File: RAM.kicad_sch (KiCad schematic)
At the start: 286 parts, among them J1 Conn_01x50, J2 JTAG_01x06, J3 Conn_01x03_Male, U10 W25Q128JVS, U11 TPS62823DLC, U12 TPS62823DLC, U13 TPS62823DLC, U14 TPS62823DLC, U16 TPS62823DLC, U17 Si52112-B5-GM2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

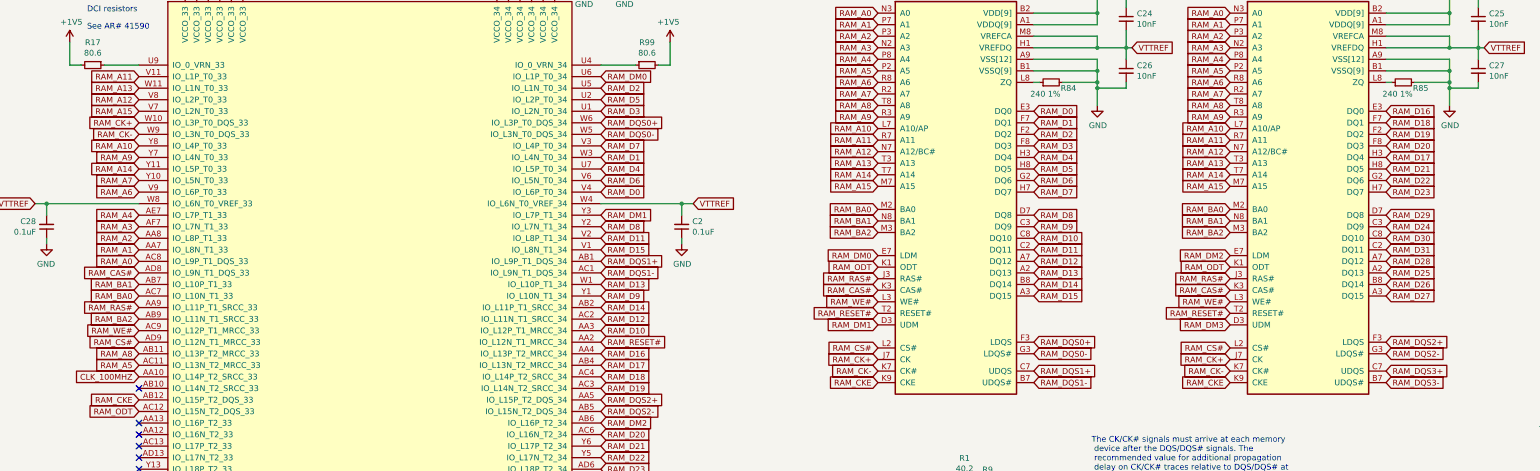
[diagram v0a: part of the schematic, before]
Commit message: ddr new routing snapshot before length matching
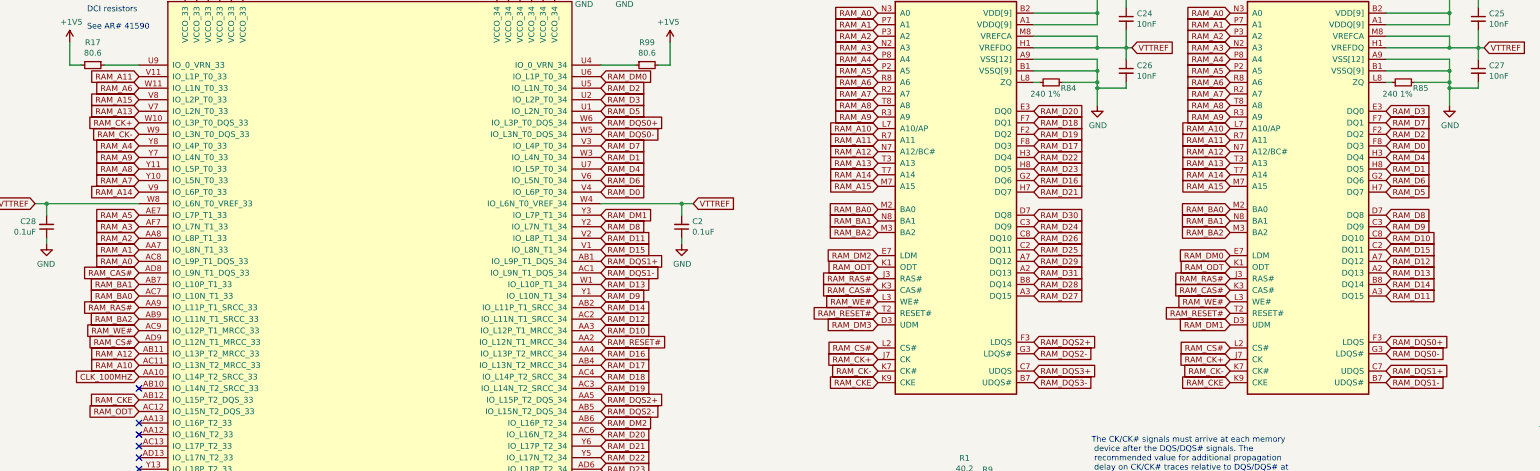
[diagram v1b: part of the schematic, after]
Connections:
- net RAM_A10: now also U2.AC11 (IO_L13N_T2_MRCC_33); no longer U2.Y8 (IO_L4P_T0_33)
- net RAM_A12: now also U2.AB11 (IO_L13P_T2_MRCC_33); no longer U2.V8 (IO_L2P_T0_33)
- net RAM_A13: now also U2.V7 (IO_L2N_T0_33); no longer U2.W11 (IO_L1N_T0_33)
- net RAM_A14: now also U2.V9 (IO_L6P_T0_33); no longer U2.Y11 (IO_L5P_T0_33)
- net RAM_A15: now also U2.V8 (IO_L2P_T0_33); no longer U2.V7 (IO_L2N_T0_33)
- net RAM_A4: now also U2.Y8 (IO_L4P_T0_33); no longer U2.AE7 (IO_L7P_T1_33)
- net RAM_A5: now also U2.AE7 (IO_L7P_T1_33); no longer U2.AC11 (IO_L13N_T2_MRCC_33)
- net RAM_A6: now also U2.W11 (IO_L1N_T0_33); no longer U2.V9 (IO_L6P_T0_33)
- net RAM_A8: now also U2.Y11 (IO_L5P_T0_33); no longer U2.AB11 (IO_L13P_T2_MRCC_33)
- net RAM_D0: now also U4.F8 (DQ3); no longer U3.E3 (DQ0)
- net RAM_D1: now also U4.H8 (DQ5); no longer U3.F7 (DQ1)
- net RAM_D10: now also U4.C8 (DQ10); no longer U3.C8 (DQ10)
- net RAM_D11: now also U4.A3 (DQ15); no longer U3.C2 (DQ11)
- net RAM_D12: now also U4.A7 (DQ12); no longer U3.A7 (DQ12)
- net RAM_D13: now also U4.A2 (DQ13); no longer U3.A2 (DQ13)
- net RAM_D14: now also U4.B8 (DQ14); no longer U3.B8 (DQ14)
- net RAM_D15: now also U4.C2 (DQ11); no longer U3.A3 (DQ15)
- net RAM_D16: now also U3.G2 (DQ6); no longer U4.E3 (DQ0)
- net RAM_D17: now also U3.F8 (DQ3); no longer U4.H3 (DQ4)
- net RAM_D18: now also U3.F7 (DQ1); no longer U4.F7 (DQ1)
- net RAM_D19: now also U3.F2 (DQ2); no longer U4.F2 (DQ2)
- net RAM_D2: now also U4.F2 (DQ2); no longer U3.F2 (DQ2)
- net RAM_D20: now also U3.E3 (DQ0); no longer U4.F8 (DQ3)
- net RAM_D21: now also U3.H7 (DQ7); no longer U4.H8 (DQ5)
- net RAM_D22: now also U3.H3 (DQ4); no longer U4.G2 (DQ6)
- net RAM_D23: now also U3.H8 (DQ5); no longer U4.H7 (DQ7)
- net RAM_D24: now also U3.C3 (DQ9); no longer U4.C3 (DQ9)
- net RAM_D25: now also U3.C2 (DQ11); no longer U4.A2 (DQ13)
- net RAM_D26: now also U3.C8 (DQ10); no longer U4.B8 (DQ14)
- net RAM_D27: now also U3.A3 (DQ15); no longer U4.A3 (DQ15)
- net RAM_D28: now also U3.B8 (DQ14); no longer U4.A7 (DQ12)
- net RAM_D29: now also U3.A7 (DQ12); no longer U4.D7 (DQ8)
- net RAM_D3: now also U2.U2 (IO_L2P_T0_34), U4.E3 (DQ0); no longer U2.U1 (IO_L2N_T0_34), U3.F8 (DQ3)
- net RAM_D30: now also U3.D7 (DQ8); no longer U4.C8 (DQ10)
- net RAM_D31: now also U3.A2 (DQ13); no longer U4.C2 (DQ11)
- net RAM_D4: now also U4.H3 (DQ4); no longer U3.H3 (DQ4)
- net RAM_D5: now also U2.U1 (IO_L2N_T0_34), U4.H7 (DQ7); no longer U2.U2 (IO_L2P_T0_34), U3.H8 (DQ5)
- net RAM_D6: now also U4.G2 (DQ6); no longer U3.G2 (DQ6)
- net RAM_D7: now also U4.F7 (DQ1); no longer U3.H7 (DQ7)
- net RAM_D8: now also U4.D7 (DQ8); no longer U3.D7 (DQ8)
- net RAM_D9: now also U4.C3 (DQ9); no longer U3.C3 (DQ9)
- net RAM_DM0: now also U4.E7 (LDM); no longer U3.E7 (LDM)
- net RAM_DM1: now also U4.D3 (UDM); no longer U3.D3 (UDM)
- net RAM_DM2: now also U3.E7 (LDM); no longer U4.E7 (LDM)
- net RAM_DM3: now also U3.D3 (UDM); no longer U4.D3 (UDM)
- net RAM_DQS0+: now also U4.F3 (LDQS); no longer U3.F3 (LDQS)
- net RAM_DQS0-: now also U4.G3 (LDQS#); no longer U3.G3 (LDQS#)
- net RAM_DQS1+: now also U4.C7 (UDQS); no longer U3.C7 (UDQS)
- net RAM_DQS1-: now also U4.B7 (UDQS#); no longer U3.B7 (UDQS#)
- net RAM_DQS2+: now also U3.F3 (LDQS); no longer U4.F3 (LDQS)
- net RAM_DQS2-: now also U3.G3 (LDQS#); no longer U4.G3 (LDQS#)
- net RAM_DQS3+: now also U3.C7 (UDQS); no longer U4.C7 (UDQS)
- net RAM_DQS3-: now also U3.B7 (UDQS#); no longer U4.B7 (UDQS#)

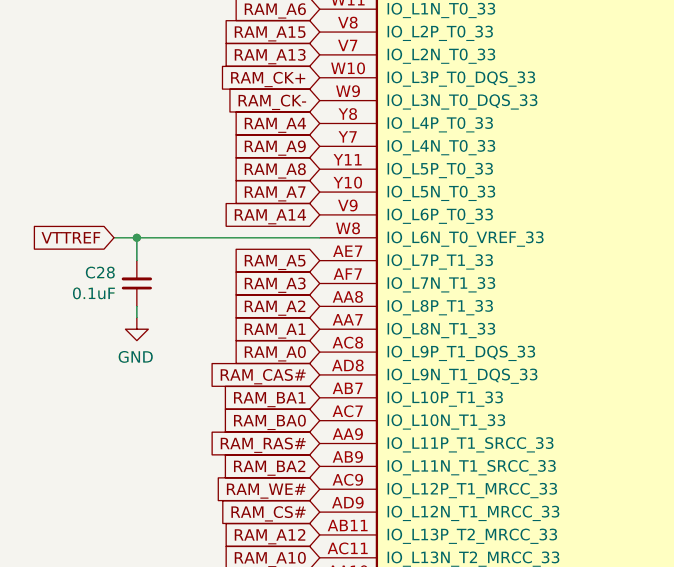
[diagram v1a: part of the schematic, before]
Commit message: ddr new routing snapshot after length matching
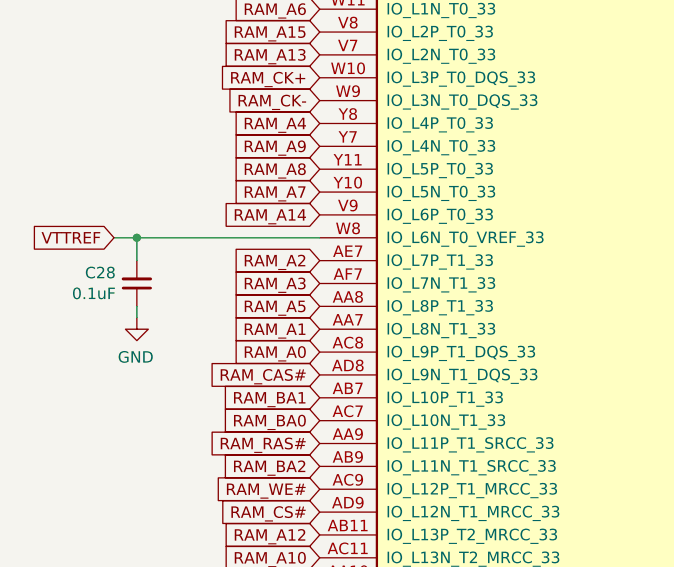
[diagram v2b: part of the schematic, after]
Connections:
- net RAM_A2: now also U2.AE7 (IO_L7P_T1_33); no longer U2.AA8 (IO_L8P_T1_33)
- net RAM_A5: now also U2.AA8 (IO_L8P_T1_33); no longer U2.AE7 (IO_L7P_T1_33)
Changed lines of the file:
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@@
     )
   )
-  (global_label "RAM_A5" (shape input) (at 76.2 312.42 180) (fields_autoplaced)
-    (effects (font (size 1.27 1.27)) (justify right))
-    (property "Intersheet References" "${INTERSHEET_REFS}" (id 0) (at 0 -33.02 0)
+  (global_label "RAM_A5" (shape input) (at 76.2 317.5 180) (fields_autoplaced)
+    (effects (font (size 1.27 1.27)) (justify right))
+    (property "Intersheet References" "${INTERSHEET_REFS}" (id 0) (at 0 -27.94 0)
       (effects (font (size 1.27 1.27)) hide)
     )
@@
     )
   )
-  (global_label "RAM_A2" (shape input) (at 76.2 317.5 180) (fields_autoplaced)
-    (effects (font (size 1.27 1.27)) (justify right))
-    (property "Intersheet References" "${INTERSHEET_REFS}" (id 0) (at 0 0 0)
-      (effects (font (size 1.27 1.27)) hide)
-    )
+  (global_label "RAM_A2" (shape input) (at 76.2 312.42 180) (fields_autoplaced)
+    (effects (font (size 1.27 1.27)) (justify right))
+    (property "Intersheet References" "${INTERSHEET_REFS}" (id 0) (at 0 -5.08 0)
+      (effects (font (size 1.27 1.27)) hide)
+    )

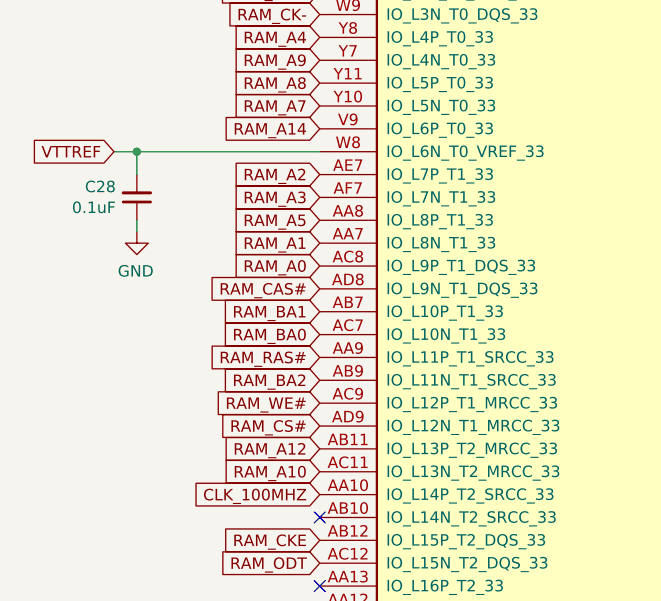
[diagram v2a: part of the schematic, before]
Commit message: snapshot with tuned ddr address/command group
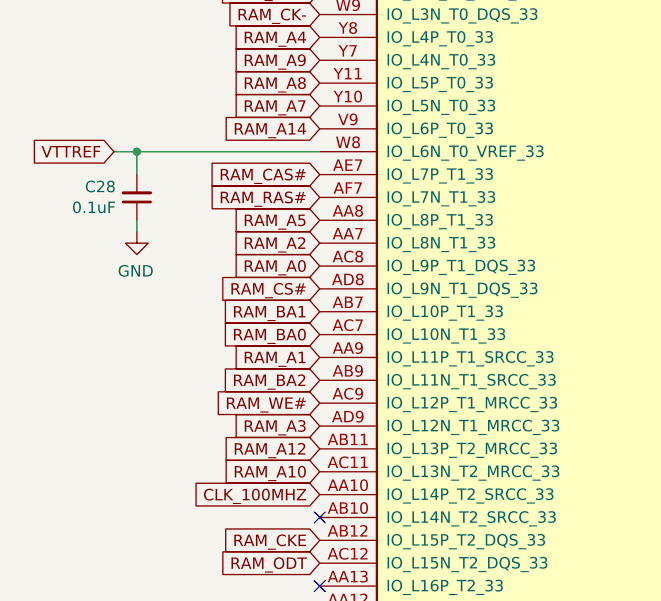
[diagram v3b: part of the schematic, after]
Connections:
- net RAM_A1: now also U2.AA9 (IO_L11P_T1_SRCC_33); no longer U2.AA7 (IO_L8N_T1_33)
- net RAM_A2: now also U2.AA7 (IO_L8N_T1_33); no longer U2.AE7 (IO_L7P_T1_33)
- net RAM_A3: now also U2.AD9 (IO_L12N_T1_MRCC_33); no longer U2.AF7 (IO_L7N_T1_33)
- net RAM_CAS#: now also U2.AE7 (IO_L7P_T1_33); no longer U2.AD8 (IO_L9N_T1_DQS_33)
- net RAM_CS#: now also U2.AD8 (IO_L9N_T1_DQS_33); no longer U2.AD9 (IO_L12N_T1_MRCC_33)
- net RAM_RAS#: now also U2.AF7 (IO_L7N_T1_33); no longer U2.AA9 (IO_L11P_T1_SRCC_33)
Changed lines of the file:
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@@
     )
   )
-  (global_label "RAM_CS#" (shape input) (at 76.2 340.36 180) (fields_autoplaced)
-    (effects (font (size 1.27 1.27)) (justify right))
-    (property "Intersheet References" "${INTERSHEET_REFS}" (id 0) (at 0 0 0)
+  (global_label "RAM_CS#" (shape input) (at 76.2 325.12 180) (fields_autoplaced)
+    (effects (font (size 1.27 1.27)) (justify right))
+    (property "Intersheet References" "${INTERSHEET_REFS}" (id 0) (at 0 -15.24 0)
       (effects (font (size 1.27 1.27)) hide)
     )
@@
     )
   )
-  (global_label "RAM_RAS#" (shape input) (at 76.2 332.74 180) (fields_autoplaced)
-    (effects (font (size 1.27 1.27)) (justify right))
-    (property "Intersheet References" "${INTERSHEET_REFS}" (id 0) (at 0 0 0)
+  (global_label "RAM_RAS#" (shape input) (at 76.2 314.96 180) (fields_autoplaced)
+    (effects (font (size 1.27 1.27)) (justify right))
+    (property "Intersheet References" "${INTERSHEET_REFS}" (id 0) (at 0 -17.78 0)
       (effects (font (size 1.27 1.27)) hide)
     )
@@
     )
   )
-  (global_label "RAM_A1" (shape input) (at 76.2 320.04 180) (fields_autoplaced)
-    (effects (font (size 1.27 1.27)) (justify right))
-    (property "Intersheet References" "${INTERSHEET_REFS}" (id 0) (at 0 0 0)
-      (effects (font (size 1.27 1.27)) hide)
-    )
-  )
-  (global_label "RAM_CAS#" (shape input) (at 76.2 325.12 180) (fields_autoplaced)
-    (effects (font (size 1.27 1.27)) (justify right))
-    (property "Intersheet References" "${INTERSHEET_REFS}" (id 0) (at 0 0 0)
+  (global_label "RAM_A1" (shape input) (at 76.2 332.74 180) (fields_autoplaced)
+    (effects (font (size 1.27 1.27)) (justify right))
+    (property "Intersheet References" "${INTERSHEET_REFS}" (id 0) (at 0 12.7 0)
+      (effects (font (size 1.27 1.27)) hide)
+    )
+  )
+  (global_label "RAM_CAS#" (shape input) (at 76.2 312.42 180) (fields_autoplaced)
+    (effects (font (size 1.27 1.27)) (justify right))
+    (property "Intersheet References" "${INTERSHEET_REFS}" (id 0) (at 0 -12.7 0)
       (effects (font (size 1.27 1.27)) hide)
     )
@@
     )
   )
-  (global_label "RAM_A2" (shape input) (at 76.2 312.42 180) (fields_autoplaced)
-    (effects (font (size 1.27 1.27)) (justify right))
-    (property "Intersheet References" "${INTERSHEET_REFS}" (id 0) (at 0 -5.08 0)
+  (global_label "RAM_A2" (shape input) (at 76.2 320.04 180) (fields_autoplaced)
+    (effects (font (size 1.27 1.27)) (justify right))
+    (property "Intersheet References" "${INTERSHEET_REFS}" (id 0) (at 0 2.54 0)
       (effects (font (size 1.27 1.27)) hide)
     )
@@
     )
   )
-  (global_label "RAM_A3" (shape input) (at 76.2 314.96 180) (fields_autoplaced)
-    (effects (font (size 1.27 1.27)) (justify right))
-    (property "Intersheet References" "${INTERSHEET_REFS}" (id 0) (at 0 0 0)
-      (effects (font (size 1.27 1.27)) hide)
-    )
+  (global_label "RAM_A3" (shape input) (at 76.2 340.36 180) (fields_autoplaced)
+    (effects (font (size 1.27 1.27)) (justify right))
+    (property "Intersheet References" "${INTERSHEET_REFS}" (id 0) (at 0 25.4 0)
+      (effects (font (size 1.27 1.27)) hide)
+    )

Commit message: snapshot after cleanup
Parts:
- removed C31, C34: 10uF, symbol Device:C_Small
- removed C32: 0.1uF, Capacitor_SMD:C_0402_1005Metric, symbol Device:C_Small
- removed C33: 3.3nF, Capacitor_SMD:C_0402_1005Metric, symbol Device:C_Small
- removed L7: IHLP1212AEERR47M11, Inductor_SMD:L_Vishay_IHLP-1212, symbol Device:L_Small
- removed R52, R56: 100k 1%, Resistor_SMD:R_0402_1005Metric, symbol Device:R_Small
- removed R53: 32k 1%, Resistor_SMD:R_0402_1005Metric, symbol Device:R_Small
- removed U7: TPS62131, Package_DFN_QFN:VQFN-16-1EP_3x3mm_P0.5mm_EP1.68x1.68mm_ThermalVias, symbol Regulator_Switching:TPS62131
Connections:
- net +1V2: no longer J1.35 (Pin_35), J1.36 (Pin_36)
- net +1V8: now also J1.35 (Pin_35), J1.36 (Pin_36)
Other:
- note removed: "2.2uH?"
- note removed: "22uF?"
- note removed: "Formula: R1 = R2 x (Vout/0.8 - 1) R2 should not exceed 400 kΩ"

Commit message: first finished layout of rev 2
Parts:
- added C15, C31, C32: 0.1uF, Capacitor_SMD:C_0402_1005Metric, symbol Device:C_Small
- added R44, R45: 0, Resistor_SMD:R_0402_1005Metric, symbol Device:R_Small
- added R52, R53: 100k 1%, Resistor_SMD:R_0402_1005Metric, symbol Device:R_Small
- added TP10, TP11, TP12, TP14, TP15, TP16, TP2, TP8, TP9: TestPoint, TestPoint:TestPoint_Pad_1.0x1.0mm, symbol Connector:TestPoint
- J2: footprint Connector_PinHeader_2.00mm:PinHeader_1x06_P2.00mm_Horizontal -> Connector_PinHeader_2.00mm:PinHeader_1x06_P2.00mm_Vertical
- J3: footprint Connector_PinHeader_2.00mm:PinHeader_1x03_P2.00mm_Horizontal -> Connector_PinHeader_2.00mm:PinHeader_1x03_P2.00mm_Vertical
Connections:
- net +5V: now also R52.1, R53.1
- net DISP2_GPIO0: now also U2.N21 (IO_L12P_T1_MRCC_13)
- net DISP2_GPIO1: now also U2.N19 (IO_L7P_T1_13)
- net DISP2_GPIO2: now also U2.M19 (IO_L22N_T3_13)
- net DISP2_GPIO3: now also U2.M20 (IO_L7N_T1_13)
- net DISP2_GPIO4: now also U2.M21 (IO_L10P_T1_13)
- net DISP2_GPIO5: now also U2.M22 (IO_L10N_T1_13)
- net EN_VDDR: now also R52.2
- net EN_VIO: now also R53.2
- net GND: now also C32.2, TP16.1
- net USB1_RX_P: now reaches U2.K25 (IO_L1P_T0_13)
- net USB1_RX_N: now reaches U2.K26 (IO_L1N_T0_13)
- net USB1_C_DN: now reaches U2.L24 (IO_L8N_T1_13)
- net USB1_C_DN: now also R45.2
- net USB1_C_DP: now reaches U2.M24 (IO_L8P_T1_13)
- net USB1_C_DP: now also R44.1
- net USB1_TX_CN: now reaches U2.M26 (IO_L5N_T0_13)
- net USB1_TX_CN: now also C15.2
- net USB1_TX_CP: now reaches U2.N26 (IO_L5P_T0_13)
- net USB1_TX_CP: now also C31.2
- net TP_P21: now reaches U2.P21 (IO_L13N_T2_MRCC_13)
- net TP_P21: now also TP15.1
- net TP_P26: now reaches U2.P26 (IO_L2N_T0_13)
- net TP_P26: now also TP10.1
- net TP_R21: now reaches U2.R21 (IO_L13P_T2_MRCC_13)
- net TP_R21: now also TP14.1
- net TP_R23: now reaches U2.R23 (IO_L14N_T2_SRCC_13)
- net TP_R23: now also TP12.1
- net TP_R26: now reaches U2.R26 (IO_L2P_T0_13)
- net TP_R26: now also TP11.1
- net TP_U26: now reaches U2.U26 (IO_L4P_T0_12)
- net TP_U26: now also TP9.1
- net TP_V26: now reaches U2.V26 (IO_L4N_T0_12)
- net TP_V26: now also TP8.1
- net TP_W25: now reaches U2.W25 (IO_L5P_T0_12)
- net TP_W25: now also TP2.1
- net at R101.2, U18.3 (EN): now also C32.1
- net EN_VAUX: no longer names the net of U18.6 (FLAG1)
- new net USB1_DN: R45.1
- new net USB1_DP: R44.2
- new net USB1_TX_N: C15.1
- new net USB1_TX_P: C31.1
- no-connect marks 183 -> 180
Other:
- note added: "POWERUP SEQUENCER"
- note added: "TODO: might need to SWAP a SATA pair!?!"
- note removed: "TODO: resolve bodges"
- note removed: "ball assignments checked, except power"
- moved on the sheet: R101, U18

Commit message: pcb: clean up D-2 BOM
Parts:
- added R46: 1.5k, Resistor_SMD:R_0402_1005Metric, symbol Device:R_Small
- C82, C89, C93, C94, C97, C98: Manufacturer (none) -> Generic; Manufacturer_No (none) -> 0603 10V+
- D1, D2: Manufacturer (none) -> Generic; Manufacturer_No (none) -> WLED 0603
- FB1, FB2, FB3: Manufacturer (none) -> Murata; Manufacturer_No (none) -> 100ohms @ 100MHz 0603
- GFX2: footprint footprints:mnt-rkx7-badge-d01 -> footprints:mnt-rkx7-badge-d02
- J1: Manufacturer (none) -> Hirose; Manufacturer_No (none) -> FH12-50S-0.5SH
- R101, R32, R35, R38, R41, R47: Manufacturer (none) -> Yageo; Manufacturer_No (none) -> AC0402FR-070RL
- R36: Manufacturer (none) -> Vishay Dale; Manufacturer_No (none) -> CRCW0402100KFKEDC
- R37: Manufacturer Vishay Dale -> Yageo; Manufacturer_No CRCW0402100KFKEDC -> RE0402DRE07150KL
- R44, R45: value 0 -> 20
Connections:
- net USB1_C_DN: now also U2.C26 (IO_L5N_T0_D07_14); no longer U2.L24 (IO_L8N_T1_13)
- net USB1_C_DP: now also U2.D26 (IO_L5P_T0_D06_14), R46.1; no longer U2.M24 (IO_L8P_T1_13)
- net USB1_PULL: now reaches U2.F25 (IO_L17P_T2_A14_D30_14)
- net USB1_PULL: now also R46.2
- no-connect marks 180 -> 220
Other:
- note added: "TODO: - [x] FPC port to ANX9807 - [x] wire up USB host directly and confirm LiteX compat. - test SATA with existing module - test audio with existing module"
- note removed: "TODO: - [ ] FPC port to ANX9807 - rest of powers - [ ] wire up USB host directly and confirm LiteX compat. - test SATA with existing module? - test audio with existing module"
- note removed: "TODO: according to ddr4 test board"
- note removed: "TODO: can i use this?"
- note removed: "TODO: caps needed?"
- note removed: "TODO: double check"
- note removed: "TODO: hook up gpios"
- note removed: "TODO: might need to SWAP a SATA pair!?!"
- moved on the sheet: C15, C31, R44, R45
